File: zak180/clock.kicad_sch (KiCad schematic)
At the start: 15 parts, among them Q2 BC547, SW1 Reset, U18 NE555P, U19 74HC163, X1 25.175 MHz

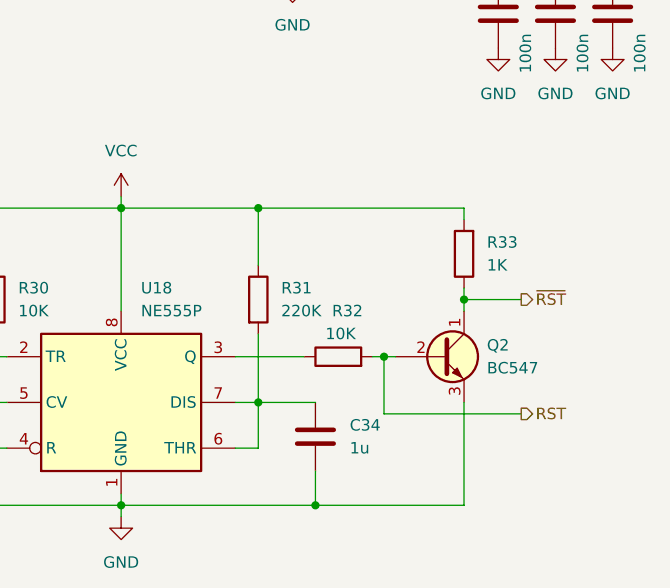
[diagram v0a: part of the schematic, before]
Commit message: HW: Fix RST line
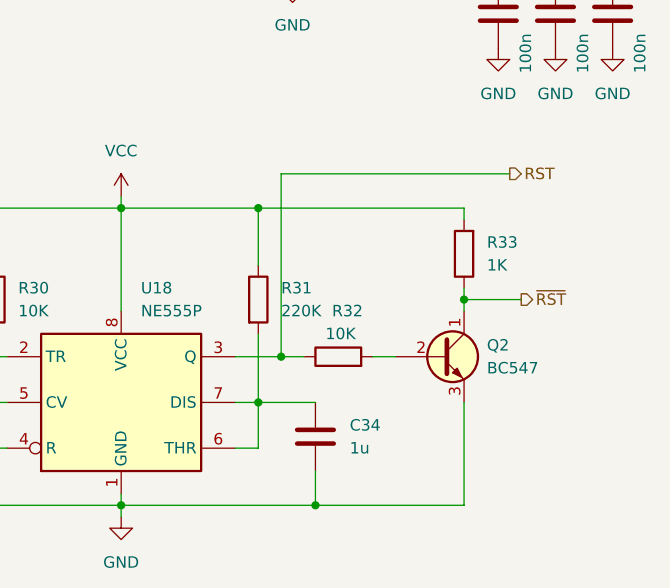
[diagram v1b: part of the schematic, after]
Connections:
- net RST: now also R32.1, U18.3 (Q); no longer Q2.2 (B), R32.2
- new net: Q2.2 (B), R32.2
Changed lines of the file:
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@@
-	)
-	(junction
-		(at 163.83 124.46)
-		(diameter 0)
-		(color 0 0 0 0)
 	)
 	(junction
@@
 	)
 	(junction
+		(at 152.4 124.46)
+		(diameter 0)
+		(color 0 0 0 0)
+	)
+	(junction
 		(at 139.7 54.61)
 		(diameter 0)
@@
 	(wire
 		(pts
-			(xy 163.83 124.46) (xy 163.83 130.81)
-		)
-		(stroke
-			(width 0)
-			(type default)
-		)
-	)
-	(wire
-		(pts
 			(xy 149.86 107.95) (xy 172.72 107.95)
 		)
@@
 	(wire
 		(pts
+			(xy 152.4 104.14) (xy 152.4 124.46)
+		)
+		(stroke
+			(width 0)
+			(type default)
+		)
+	)
+	(wire
+		(pts
 			(xy 170.18 57.15) (xy 166.37 57.15)
 		)
@@
 	(wire
 		(pts
-			(xy 163.83 130.81) (xy 179.07 130.81)
-		)
-		(stroke
-			(width 0)
-			(type default)
-		)
-	)
-	(wire
-		(pts
 			(xy 139.7 52.07) (xy 139.7 54.61)
 		)
@@
 	(wire
 		(pts
-			(xy 162.56 124.46) (xy 163.83 124.46)
+			(xy 162.56 124.46) (xy 165.1 124.46)
 		)
 		(stroke
@@
 	(wire
 		(pts
+			(xy 152.4 124.46) (xy 154.94 124.46)
+		)
+		(stroke
+			(width 0)
+			(type default)
+		)
+	)
+	(wire
+		(pts
 			(xy 139.7 54.61) (xy 140.97 54.61)
 		)
@@
 	(wire
 		(pts
-			(xy 163.83 124.46) (xy 165.1 124.46)
-		)
-		(stroke
-			(width 0)
-			(type default)
-		)
-	)
-	(wire
-		(pts
 			(xy 121.92 124.46) (xy 120.65 124.46)
 		)
@@
 	(wire
 		(pts
+			(xy 177.8 104.14) (xy 152.4 104.14)
+		)
+		(stroke
+			(width 0)
+			(type default)
+		)
+	)
+	(wire
+		(pts
 			(xy 127 81.28) (xy 127 69.85)
 		)
@@
 	(wire
 		(pts
-			(xy 147.32 124.46) (xy 154.94 124.46)
+			(xy 147.32 124.46) (xy 152.4 124.46)
 		)
 		(stroke
@@
 	(hierarchical_label "RST"
 		(shape output)
-		(at 179.07 130.81 0)
+		(at 177.8 104.14 0)
 		(fields_autoplaced yes)
 		(effects
